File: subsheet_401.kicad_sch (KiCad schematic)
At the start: 21 parts, among them J2001 For RGB2HDMI, U401 STE_GSTSHIFTER_PHY

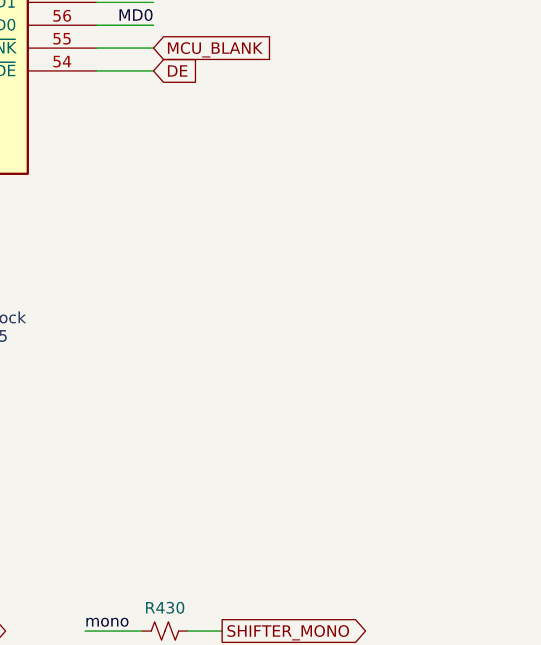
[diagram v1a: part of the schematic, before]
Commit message: add gnd/vcc symbol to start replacing local labels
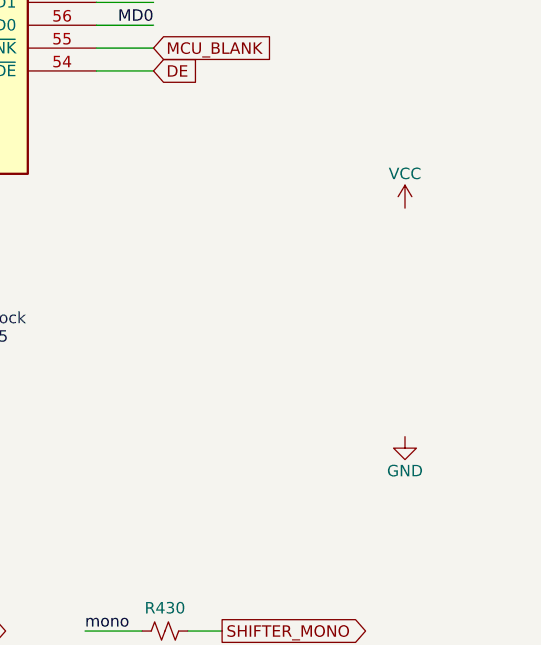
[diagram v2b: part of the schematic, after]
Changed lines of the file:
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@@
     )
   )
+  (symbol (lib_id "power:VCC") (at 181.61 143.51 0) (unit 1)
+    (in_bom yes) (on_board yes)
+    (property "Reference" "#PWR?" (id 0) (at 181.61 147.32 0)
+      (effects (font (size 1.27 1.27)) hide)
+    )
+    (property "Value" "VCC" (id 1) (at 181.61 139.7 0))
+    (property "Footprint" "" (id 2) (at 181.61 143.51 0)
+      (effects (font (size 1.27 1.27)) hide)
+    )
+    (property "Datasheet" "" (id 3) (at 181.61 143.51 0)
+      (effects (font (size 1.27 1.27)) hide)
+    )
+    (pin "1")
+  )
+  (symbol (lib_id "power:GND") (at 181.61 168.91 0) (unit 1)
+    (in_bom yes) (on_board yes)
+    (property "Reference" "#PWR?" (id 0) (at 181.61 175.26 0)
+      (effects (font (size 1.27 1.27)) hide)
+    )
+    (property "Value" "GND" (id 1) (at 181.61 172.72 0))
+    (property "Footprint" "" (id 2) (at 181.61 168.91 0)
+      (effects (font (size 1.27 1.27)) hide)
+    )
+    (property "Datasheet" "" (id 3) (at 181.61 168.91 0)
+      (effects (font (size 1.27 1.27)) hide)
+    )
+    (pin "1")
+  )
 )
